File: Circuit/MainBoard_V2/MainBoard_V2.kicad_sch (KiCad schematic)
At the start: 122 parts, among them J1 Conn_01x02, J10 Conn_01x03, J11 Conn_01x03, J12 Conn_01x03, J13 Conn_01x04, J14 Conn_01x04, J15 Conn_01x04, J16 Conn_01x04, J17 Conn_01x04, J18 Conn_01x02, J19 Conn_01x02, J2 Conn_01x02, J20 Conn_01x02, J21 Conn_01x02, J3 Conn_01x02, J4 Conn_01x04, J5 Conn_01x02, J6 Conn_01x02, J7 Conn_01x02, J8 Conn_01x07, J9 Raspberry_Pi_2_3, Q1 Q_PMOS_GDS, Q2 Q_PMOS_GDS, Q3 BSS138, Q4 BSS138, Q5 BSS138, Q6 BSS138, Q7 BSS138, SW1 SW_Push, SW2 SW_Push, SW3 SW_Push, SW4 SW_Slide_DPDT, SW5 SW_Slide_DPDT, U1 STM32F446RETx, U2 LM1117MP-3.3, U3 MPU-6050, Y1 CSTNE16M0V530000R0

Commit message: V2完成
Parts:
- added C19: 10u, Capacitor_SMD:C_0805_2012Metric, symbol Device:C
- added R37: 10, Resistor_SMD:R_0603_1608Metric, symbol Device:R
- C6, C7: footprint Capacitor_THT:CP_Radial_D5.0mm_P2.00mm -> Capacitor_THT:CP_Radial_D6.3mm_P2.50mm
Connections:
- net +3V3: now also C19.2
- net +5V: now also MD1.5 (SENSE)
- net BUZZER: now also U1.55 (PB3)
- net ECHO1: now also U1.50 (PA15); no longer U1.45 (PA12)
- net GND: now also MD1.1 (~{ON}/OFF_CONTROL), R4.2, C19.1, R37.2; no longer R9.1
- net TRIG1: now also U1.51 (PC10); no longer U1.50 (PA15)
- net TRIG2: now also U1.45 (PA12); no longer U1.44 (PA11)
- net TX3 renamed LIDAR_OUT
- net LIDAR_OUT: now also U1.44 (PA11); no longer U1.51 (PC10)
- new net: R37.1, R9.1
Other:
- moved on the sheet: R8, R9

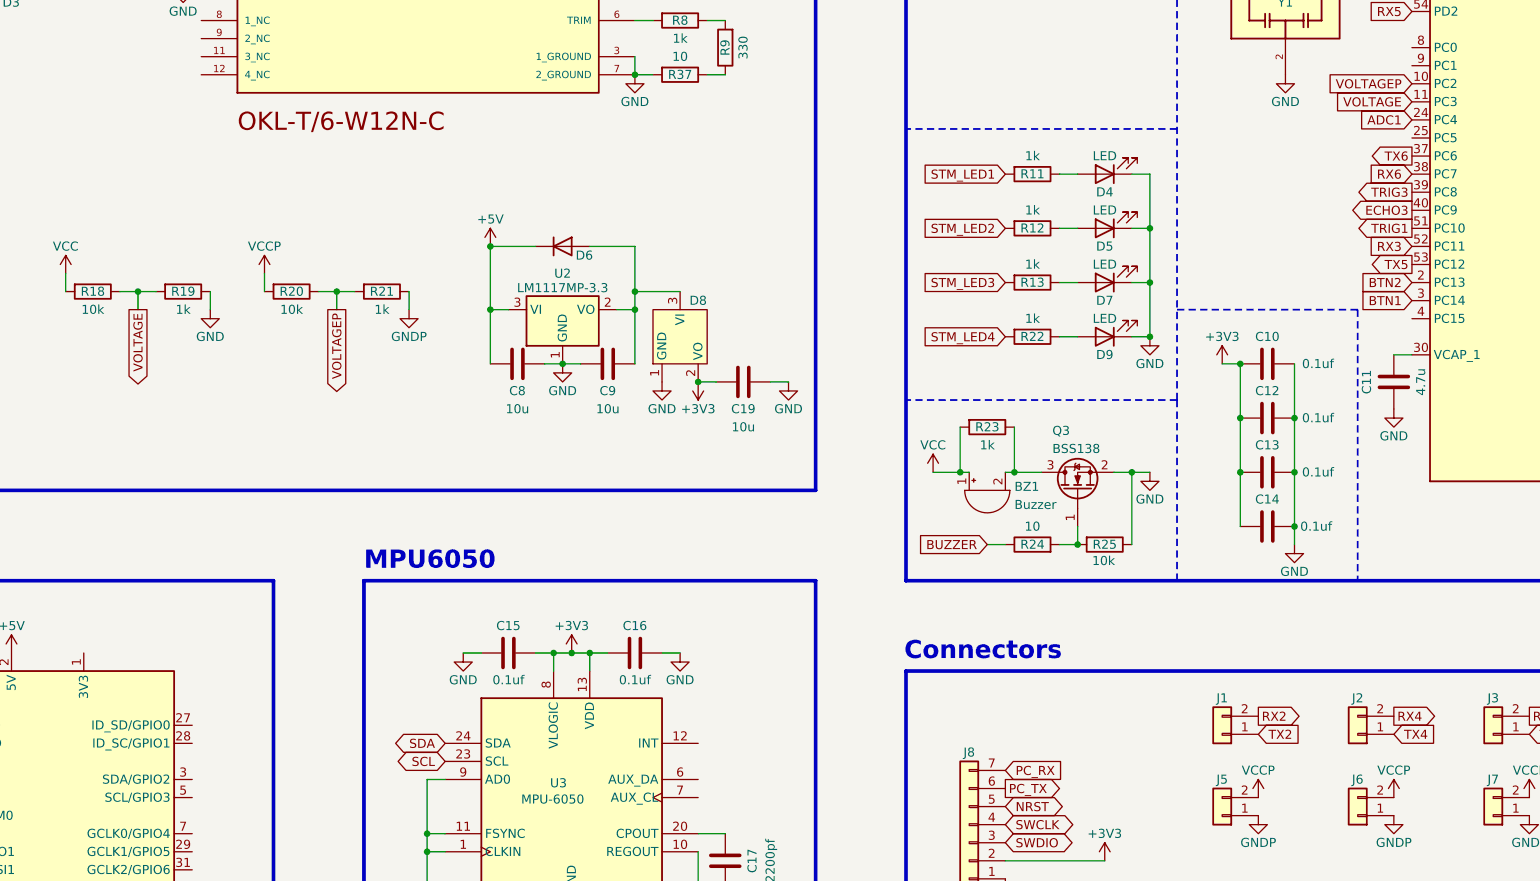
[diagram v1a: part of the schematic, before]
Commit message: Update MainBoard V2 production files
- Updated BOM to include additional capacitors (C20, C21) with increased quantities.
- Added new designators for capacitors C20 and C21 in designators.csv.
- Modified netlist.ipc to reflect changes in the circuit layout, including new connections and adjustments to existing vias.
- Adjusted positions.csv for precise component placement, including minor adjustments to several components' coordinates.
- Added a backup of the MainBoard V2 design from May 7, 2026.
- Updated the MainBoard V2 production zip file with the latest design files.
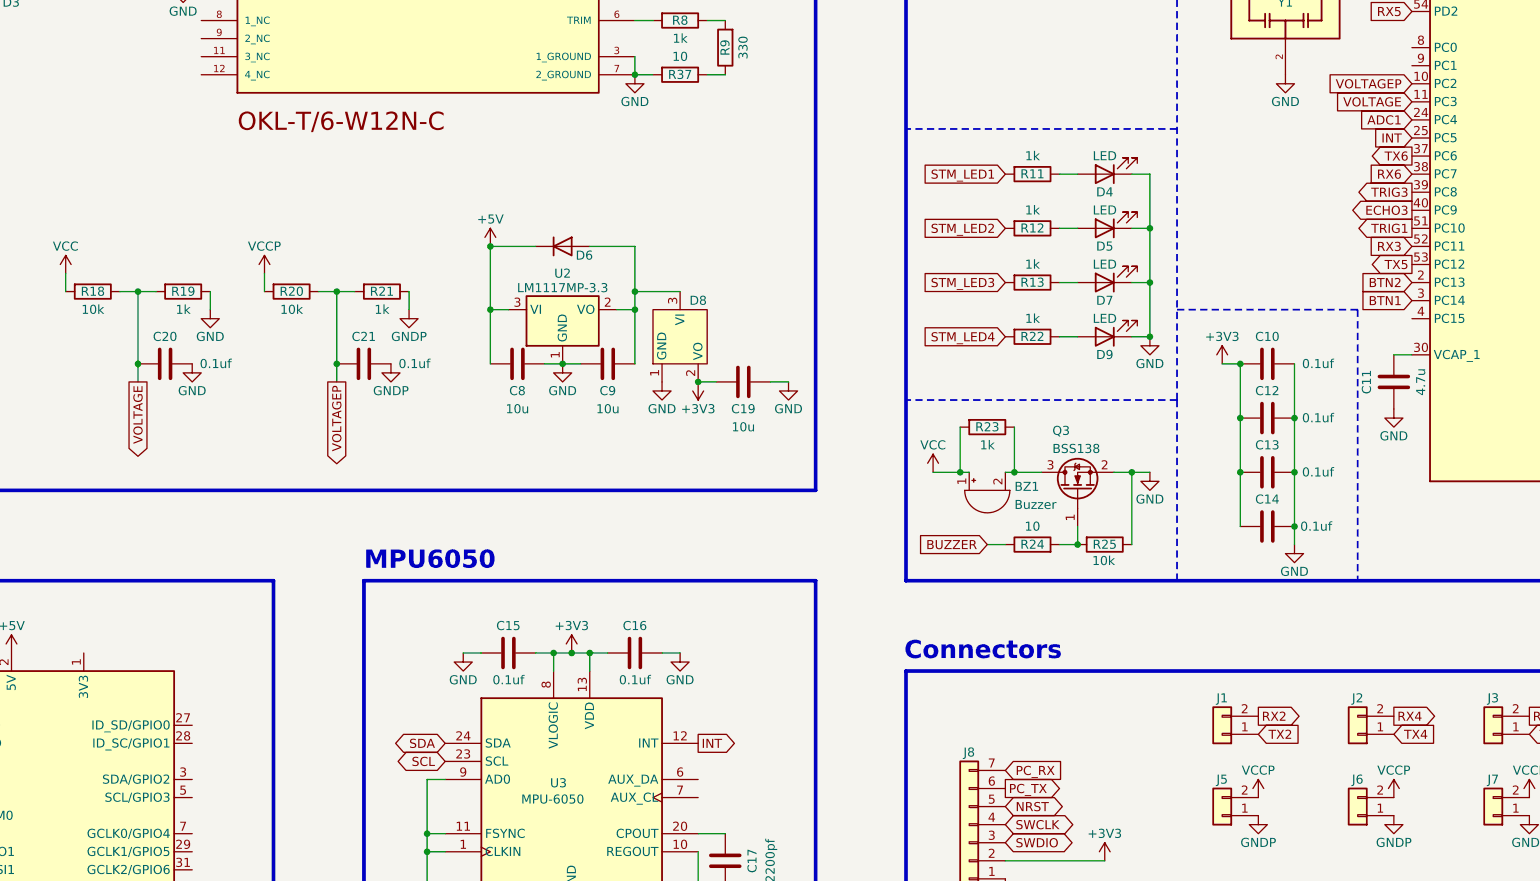
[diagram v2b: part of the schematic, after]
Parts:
- added C20, C21: 0.1uf, Capacitor_SMD:C_0603_1608Metric, symbol Device:C
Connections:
- net GND: now also C20.1
- net GNDP: now also C21.1
- net VOLTAGE: now also C20.2
- net VOLTAGEP: now also C21.2
- net INT: now reaches U1.25 (PC5)
- net INT: now also U3.12 (INT)

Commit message: ゾーン修正
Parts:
- added C22, C24, C25: 10u, Capacitor_SMD:C_0805_2012Metric, symbol Device:C
- added C23: 0.1uf, Capacitor_SMD:C_0603_1608Metric, symbol Device:C
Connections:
- net +5V: now also C22.1, C23.1, C24.1
- net BUZZER: now also J9.12 (GPIO18/PWM0)
- net GND: now also C22.2, C23.2, C24.2
- net GNDP: now also C5.1, C25.1; no longer C5.2
- net RAS_LED1: now also J9.35 (GPIO19/MISO1); no longer J9.32 (PWM0/GPIO12)
- net VCCP: now also C5.2, C25.2; no longer C5.1
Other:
- moved on the sheet: C4, C5, C6, C7, D2, D3, F1, F2, Q1, Q2, R6, R7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

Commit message: 発注
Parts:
- added C26: 10u, Capacitor_SMD:C_0805_2012Metric, symbol Device:C
- U3: footprint Sensor_Motion:InvenSense_QFN-24_4x4mm_P0.5mm -> Package_DFN_QFN:QFN-24-1EP_4x4mm_P0.5mm_EP2.15x2.15mm
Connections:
- net +3V3: now also C26.1
- net GND: now also C26.2
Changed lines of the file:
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@@
 	)
 	(junction
+		(at 275.59 100.33)
+		(diameter 0)
+		(color 0 0 0 0)
+	)
+	(junction
 		(at 283.21 132.08)
 		(diameter 0)
@@
 	)
 	(junction
+		(at 283.21 109.22)
+		(diameter 0)
+		(color 0 0 0 0)
+	)
+	(junction
 		(at 120.65 109.22)
 		(diameter 0)
@@
 	(polyline
 		(pts
-			(xy 292.1 101.6) (xy 266.7 101.6)
+			(xy 293.37 93.98) (xy 267.97 93.98)
 		)
 		(stroke
@@
 	(polyline
 		(pts
-			(xy 292.1 101.6) (xy 292.1 139.7)
+			(xy 293.37 93.98) (xy 293.37 139.7)
 		)
 		(stroke
@@
 	(wire
 		(pts
+			(xy 275.59 100.33) (xy 275.59 109.22)
+		)
+		(stroke
+			(width 0)
+			(type default)
+		)
+	)
+	(wire
+		(pts
 			(xy 161.29 187.96) (xy 161.29 177.8)
 		)
@@
 	(wire
 		(pts
+			(xy 283.21 100.33) (xy 283.21 109.22)
+		)
+		(stroke
+			(width 0)
+			(type default)
+		)
+	)
+	(wire
+		(pts
 			(xy 195.58 45.72) (xy 190.5 45.72)
 		)
@@
 	(wire
 		(pts
-			(xy 273.05 109.22) (xy 275.59 109.22)
+			(xy 273.05 100.33) (xy 275.59 100.33)
 		)
 		(stroke
@@
 	(symbol
 		(lib_id "power:+3V3")
-		(at 273.05 109.22 0)
+		(at 273.05 100.33 0)
 		(unit 1)
 		(exclude_from_sim no)
@@
 		(dnp no)
 		(property "Reference" "#PWR038"
-			(at 273.05 113.03 0)
+			(at 273.05 104.14 0)
 			(effects
 				(font
@@
 		)
 		(property "Value" "+3V3"
-			(at 273.05 105.41 0)
+			(at 273.05 96.52 0)
 			(effects
 				(font
@@
 		)
 		(property "Footprint" ""
-			(at 273.05 109.22 0)
+			(at 273.05 100.33 0)
 			(effects
 				(font
@@
 		)
 		(property "Datasheet" ""
-			(at 273.05 109.22 0)
+			(at 273.05 100.33 0)
 			(effects
 				(font
@@
 		)
 		(property "Description" "Power symbol creates a global label with name \"+3V3\""
-			(at 273.05 109.22 0)
+			(at 273.05 100.33 0)
 			(effects
 				(font
@@
 	)
 	(symbol
+		(lib_id "Device:C")
+		(at 279.4 100.33 90)
+		(mirror x)
+		(unit 1)
+		(exclude_from_sim no)
+		(in_bom yes)
+		(on_board yes)
+		(dnp no)
+		(property "Reference" "C26"
+			(at 279.4 96.52 90)
+			(effects
+				(font
+					(size 1.27 1.27)
+				)
+			)
+		)
+		(property "Value" "10u"
+			(at 284.48 100.33 90)
+			(effects
+				(font
+					(size 1.27 1.27)
+				)
+				(justify right)
+			)
+		)
+		(property "Footprint" "Capacitor_SMD:C_0805_2012Metric"
+			(at 283.21 101.2952 0)
+			(effects
+				(font
+					(size 1.27 1.27)
+				)
+				(hide yes)
+			)
+		)
+		(property "Datasheet" "~"
+			(at 279.4 100.33 0)
+			(effects
+				(font
+					(size 1.27 1.27)
+				)
+				(hide yes)
+			)
+		)
+		(property "Description" "Unpolarized capacitor"
+			(at 279.4 100.33 0)
+			(effects
+				(font
+					(size 1.27 1.27)
+				)
+				(hide yes)
+			)
+		)
+		(pin "1"
+		)
+		(pin "2"
+		)
+		(instances
+			(project "MainBoard_V2"
+				(path "/e803236c-2d70-40fc-8b05-dbcd330310d8"
+					(reference "C26")
+					(unit 1)
+				)
+			)
+		)
+	)
+	(symbol
 		(lib_id "power:VCC")
 		(at 316.23 170.18 0)
@@
 			)
 		)
-		(property "Footprint" "Sensor_Motion:InvenSense_QFN-24_4x4mm_P0.5mm"
+		(property "Footprint" "Package_DFN_QFN:QFN-24-1EP_4x4mm_P0.5mm_EP2.15x2.15mm"
 			(at 181.61 190.5 0)
 			(effects
